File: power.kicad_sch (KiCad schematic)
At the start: 13 parts, among them J3 Barrel_Jack_Switch_Pin3Ring, U3 LD1117S33TR_SOT223, U7 AP62150Z6

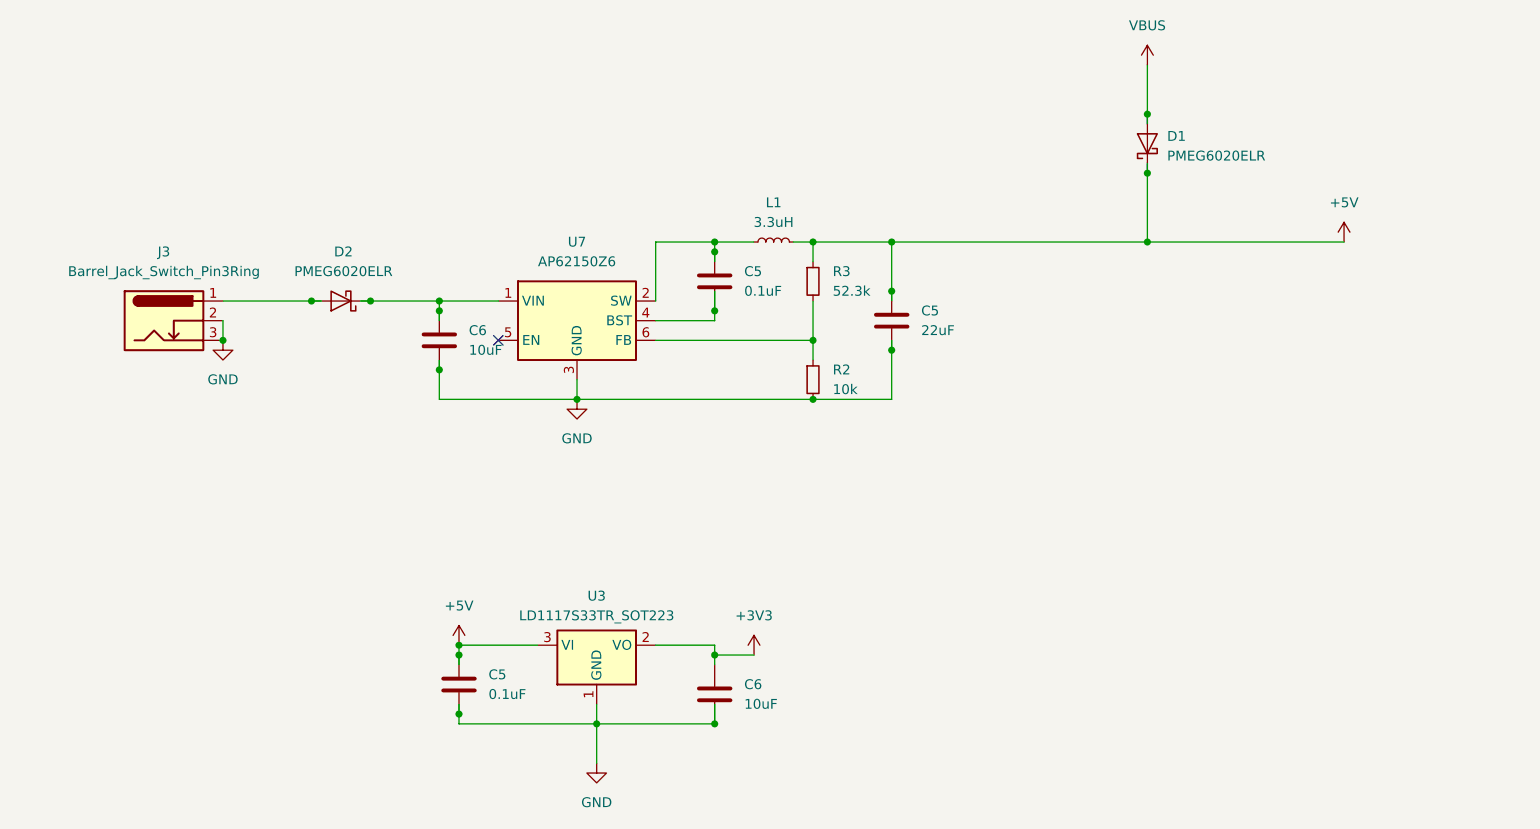
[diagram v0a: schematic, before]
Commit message: schem: update power sheet with L6981 3.3V buck converter
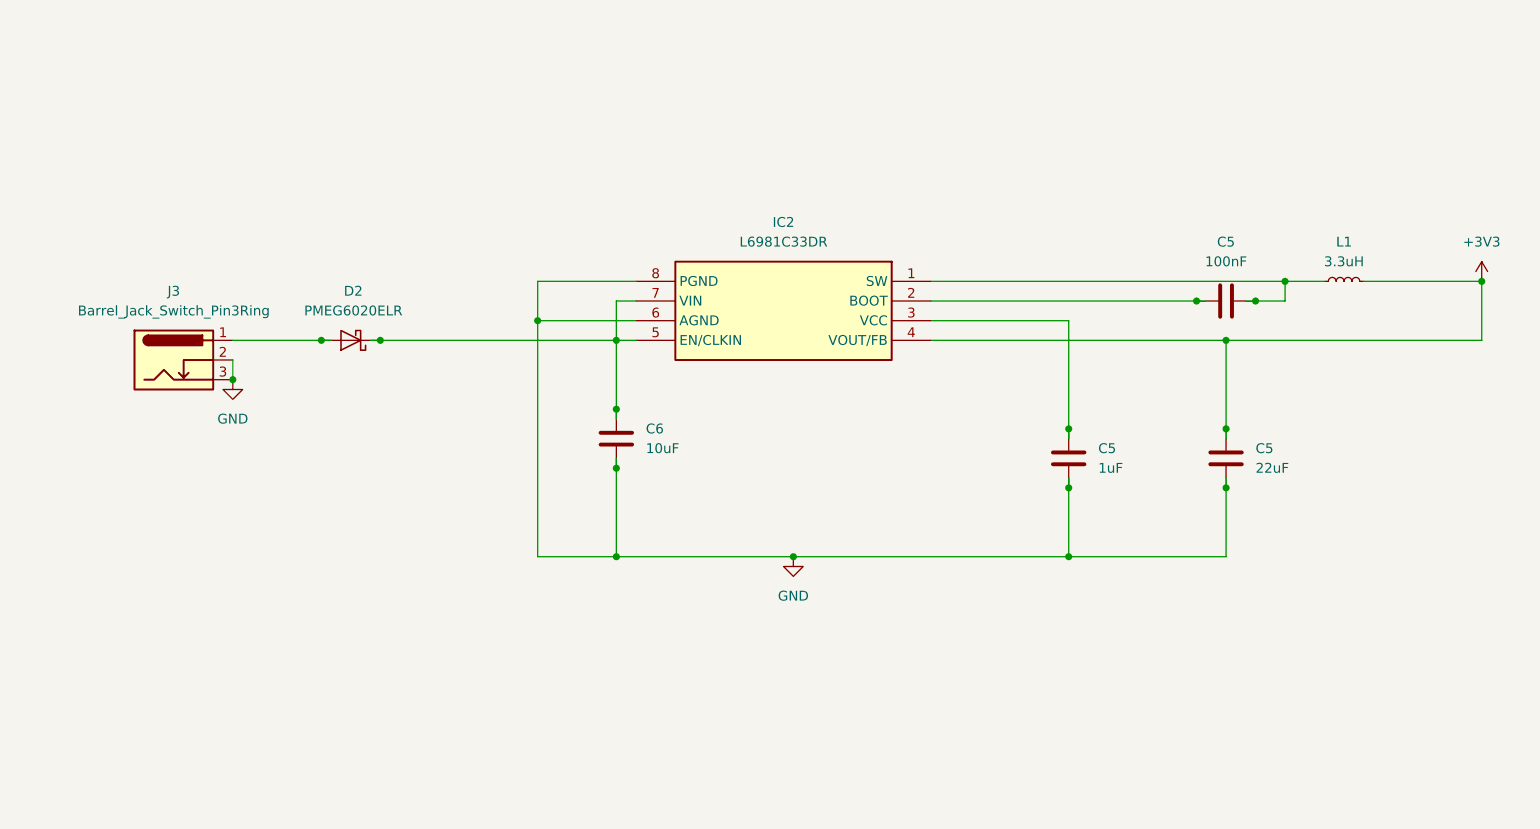
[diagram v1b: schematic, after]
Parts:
- removed C6: 10uF, symbol Device:C
- removed D1: PMEG6020ELR, Diode_SMD:Nexperia_CFP3_SOD-123W, symbol Diode:PMEG6020ELR
- removed R2: 10k, symbol Device:R_Small
- removed R3: 52.3k, symbol Device:R_Small
- removed U3: LD1117S33TR_SOT223, Package_TO_SOT_SMD:SOT-223-3_TabPin2, symbol Regulator_Linear:LD1117S33TR_SOT223
- removed U7: AP62150Z6, Package_TO_SOT_SMD:SOT-563, symbol Regulator_Switching:AP62150Z6
- added IC2: L6981C33DR, SOIC127P600X175-8N, symbol L6981C33DR:L6981C33DR
- C5: value 0.1uF -> 22uF
- C5: value 0.1uF -> 1uF
- C5: value 22uF -> 100nF
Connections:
- net +3V3: now also C5.1, L1.2, IC2.4 (VOUT/FB)
- net GND: now also C5.2, C6.1, IC2.6 (AGND), IC2.8 (PGND); no longer C5.2, C6.2
- net at D2.1 (K): now also C6.2, IC2.5 (EN/CLKIN), IC2.7 (VIN); no longer C6.1
- net at L1.1: now also C5.2, IC2.1 (SW); no longer C5.1
- removed net +5V: C5.1, C5.1, L1.2
- new net: C5.1, IC2.2 (BOOT)
- new net: C5.1, IC2.3 (VCC)
- no-connect marks 1 -> 0
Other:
- moved on the sheet: C5, C6, D2, J3, L1

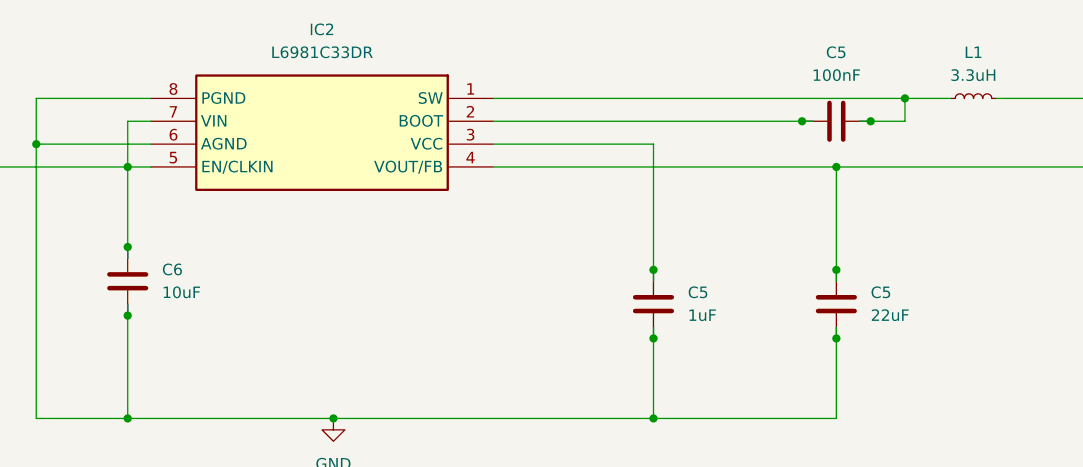
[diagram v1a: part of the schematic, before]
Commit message: feat: add esp32 component
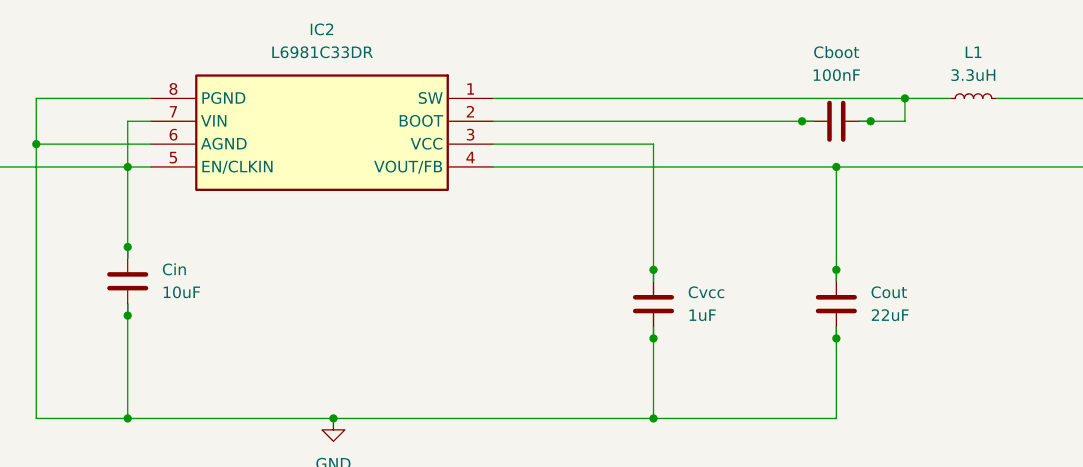
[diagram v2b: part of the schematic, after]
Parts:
- renumbered C5 to Cboot, C6 to Cin, C5 to Cout, C5 to Cvcc
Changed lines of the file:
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@@
     (instances
       (project "pv_router"
-        (path "/08ef31dc-81c2-4bcd-8336-e62c344e451e"
+        (path "/08ef31dc-81c2-4bcd-8336-e62c344e451e/760387e1-ffe6-428e-8651-2617e5a76fa2"
           (reference "J3") (unit 1)
         )
-        (path "/08ef31dc-81c2-4bcd-8336-e62c344e451e/760387e1-ffe6-428e-8651-2617e5a76fa2"
-          (reference "J3") (unit 1)
-        )
       )
     )
@@
   (symbol (lib_id "power:GND") (at 82.55 73.66 0) (unit 1)
     (in_bom yes) (on_board yes) (dnp no) (fields_autoplaced)
-    (property "Reference" "#PWR07" (at 82.55 80.01 0)
+    (property "Reference" "#PWR06" (at 82.55 80.01 0)
       (effects (font (size 1.27 1.27)) hide)
     )
@@
     (instances
       (project "pv_router"
-        (path "/08ef31dc-81c2-4bcd-8336-e62c344e451e"
-          (reference "#PWR07") (unit 1)
-        )
         (path "/08ef31dc-81c2-4bcd-8336-e62c344e451e/760387e1-ffe6-428e-8651-2617e5a76fa2"
           (reference "#PWR06") (unit 1)
@@
   (symbol (lib_id "Device:C") (at 210.82 83.82 0) (unit 1)
     (in_bom yes) (on_board yes) (dnp no) (fields_autoplaced)
-    (property "Reference" "C5" (at 214.63 82.55 0)
+    (property "Reference" "Cout" (at 214.63 82.55 0)
       (effects (font (size 1.27 1.27)) (justify left))
     )
@@
     (instances
       (project "pv_router"
-        (path "/08ef31dc-81c2-4bcd-8336-e62c344e451e"
-          (reference "C5") (unit 1)
-        )
         (path "/08ef31dc-81c2-4bcd-8336-e62c344e451e/760387e1-ffe6-428e-8651-2617e5a76fa2"
           (reference "Cout") (unit 1)
@@
   (symbol (lib_id "power:GND") (at 154.94 96.52 0) (unit 1)
     (in_bom yes) (on_board yes) (dnp no) (fields_autoplaced)
-    (property "Reference" "#PWR05" (at 154.94 102.87 0)
+    (property "Reference" "#PWR08" (at 154.94 102.87 0)
       (effects (font (size 1.27 1.27)) hide)
     )
@@
     (instances
       (project "pv_router"
-        (path "/08ef31dc-81c2-4bcd-8336-e62c344e451e"
-          (reference "#PWR05") (unit 1)
-        )
         (path "/08ef31dc-81c2-4bcd-8336-e62c344e451e/760387e1-ffe6-428e-8651-2617e5a76fa2"
           (reference "#PWR08") (unit 1)
@@
   (symbol (lib_id "Device:C") (at 190.5 83.82 0) (unit 1)
     (in_bom yes) (on_board yes) (dnp no) (fields_autoplaced)
-    (property "Reference" "C5" (at 194.31 82.55 0)
+    (property "Reference" "Cvcc" (at 194.31 82.55 0)
       (effects (font (size 1.27 1.27)) (justify left))
     )
@@
     (instances
       (project "pv_router"
-        (path "/08ef31dc-81c2-4bcd-8336-e62c344e451e"
-          (reference "C5") (unit 1)
-        )
         (path "/08ef31dc-81c2-4bcd-8336-e62c344e451e/760387e1-ffe6-428e-8651-2617e5a76fa2"
           (reference "Cvcc") (unit 1)
@@
   (symbol (lib_id "Device:C") (at 132.08 81.28 180) (unit 1)
     (in_bom yes) (on_board yes) (dnp no) (fields_autoplaced)
-    (property "Reference" "C6" (at 135.89 80.01 0)
+    (property "Reference" "Cin" (at 135.89 80.01 0)
       (effects (font (size 1.27 1.27)) (justify right))
     )
@@
     (instances
       (project "pv_router"
-        (path "/08ef31dc-81c2-4bcd-8336-e62c344e451e"
-          (reference "C6") (unit 1)
-        )
         (path "/08ef31dc-81c2-4bcd-8336-e62c344e451e/760387e1-ffe6-428e-8651-2617e5a76fa2"
           (reference "Cin") (unit 1)
@@
   (symbol (lib_id "power:+3V3") (at 243.84 60.96 0) (unit 1)
     (in_bom yes) (on_board yes) (dnp no) (fields_autoplaced)
-    (property "Reference" "#PWR04" (at 243.84 64.77 0)
+    (property "Reference" "#PWR05" (at 243.84 64.77 0)
       (effects (font (size 1.27 1.27)) hide)
     )
@@
     (instances
       (project "pv_router"
-        (path "/08ef31dc-81c2-4bcd-8336-e62c344e451e"
-          (reference "#PWR04") (unit 1)
-        )
         (path "/08ef31dc-81c2-4bcd-8336-e62c344e451e/760387e1-ffe6-428e-8651-2617e5a76fa2"
           (reference "#PWR05") (unit 1)
@@
   (symbol (lib_id "Device:C") (at 210.82 63.5 90) (unit 1)
     (in_bom yes) (on_board yes) (dnp no) (fields_autoplaced)
-    (property "Reference" "C5" (at 210.82 55.88 90)
+    (property "Reference" "Cboot" (at 210.82 55.88 90)
       (effects (font (size 1.27 1.27)))
     )
@@
     (instances
       (project "pv_router"
-        (path "/08ef31dc-81c2-4bcd-8336-e62c344e451e"
-          (reference "C5") (unit 1)
-        )
         (path "/08ef31dc-81c2-4bcd-8336-e62c344e451e/760387e1-ffe6-428e-8651-2617e5a76fa2"
           (reference "Cboot") (unit 1)

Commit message: ERC checked
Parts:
- renumbered Cboot to Cboot1, Cin to Cin1, Cout to Cout1, Cvcc to Cvcc1
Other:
- moved on the sheet: Cboot1, Cin1, Cout1, Cvcc1, J3

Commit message: PCB : add barrel jack FP
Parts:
- J3: footprint (none) -> Connector_BarrelJack:BarrelJack_Wuerth_6941xx301002
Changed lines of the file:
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@@
       (effects (font (size 1.27 1.27)))
     )
-    (property "Footprint" "" (at 72.39 72.136 0)
+    (property "Footprint" "Connector_BarrelJack:BarrelJack_Wuerth_6941xx301002" (at 72.39 72.136 0)
       (effects (font (size 1.27 1.27)) hide)
     )

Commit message: FP: assigned
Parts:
- Cboot1, Cin1, Cout1, Cvcc1: footprint (none) -> Capacitor_SMD:C_0805_2012Metric_Pad1.18x1.45mm_HandSolder
- L1: footprint (none) -> Inductor_SMD:L_10.4x10.4_H4.8
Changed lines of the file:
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@@
       (effects (font (size 1.27 1.27)) (justify left))
     )
-    (property "Footprint" "" (at 211.7852 88.9 0)
+    (property "Footprint" "Capacitor_SMD:C_0805_2012Metric_Pad1.18x1.45mm_HandSolder" (at 211.7852 88.9 0)
       (effects (font (size 1.27 1.27)) hide)
     )
@@
       (effects (font (size 1.27 1.27)) (justify left))
     )
-    (property "Footprint" "" (at 191.4652 86.36 0)
+    (property "Footprint" "Capacitor_SMD:C_0805_2012Metric_Pad1.18x1.45mm_HandSolder" (at 191.4652 86.36 0)
       (effects (font (size 1.27 1.27)) hide)
     )
@@
       (effects (font (size 1.27 1.27)) (justify right))
     )
-    (property "Footprint" "" (at 131.1148 78.74 0)
+    (property "Footprint" "Capacitor_SMD:C_0805_2012Metric_Pad1.18x1.45mm_HandSolder" (at 131.1148 78.74 0)
       (effects (font (size 1.27 1.27)) hide)
     )
@@
       (effects (font (size 1.27 1.27)))
     )
-    (property "Footprint" "" (at 215.9 62.5348 0)
+    (property "Footprint" "Capacitor_SMD:C_0805_2012Metric_Pad1.18x1.45mm_HandSolder" (at 215.9 62.5348 0)
       (effects (font (size 1.27 1.27)) hide)
     )
@@
       (effects (font (size 1.27 1.27)))
     )
-    (property "Footprint" "" (at 226.06 60.96 0)
-      (effects (font (size 1.27 1.27)) hide)
-    )
+    (property "Footprint" "Inductor_SMD:L_10.4x10.4_H4.8" (at 226.06 60.96 0)
+      (effects (font (size 1.27 1.27)) hide)
+    )
